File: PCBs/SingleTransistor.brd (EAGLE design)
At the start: 17.8 x 29.2 mm, 4 parts, among them T1 BC547N

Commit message: Updated
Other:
- board size 17.8 x 29.2 mm -> 20.5 x 32.5 mm
- board text added: "PinwheelRobotics"
- board text added: "care@pinwheel.in"
- board text removed: "Pinwheel Robotics"
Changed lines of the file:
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@@
 <drawing>
 <settings>
-<setting alwaysvectorfont="no"/>
+<setting alwaysvectorfont="yes"/>
 <setting verticaltext="up"/>
 </settings>
-<grid distance="50" unitdist="mil" unit="mm" style="lines" multiple="1" display="yes" altdistance="5" altunitdist="mil" altunit="mm"/>
+<grid distance="0.5" unitdist="mm" unit="mm" style="lines" multiple="1" display="yes" altdistance="5" altunitdist="mil" altunit="mm"/>
 <layers>
 <layer number="1" name="Top" color="4" fill="1" visible="yes" active="yes"/>
@@
 <layer number="43" name="vRestrict" color="2" fill="10" visible="yes" active="yes"/>
 <layer number="44" name="Drills" color="7" fill="1" visible="no" active="yes"/>
-<layer number="45" name="Holes" color="7" fill="1" visible="no" active="yes"/>
+<layer number="45" name="Holes" color="7" fill="1" visible="yes" active="yes"/>
 <layer number="46" name="Milling" color="3" fill="1" visible="no" active="yes"/>
 <layer number="47" name="Measures" color="7" fill="1" visible="no" active="yes"/>
@@
 <board>
 <plain>
-<wire x1="2.54" y1="12.7" x2="20.371" y2="12.7" width="0" layer="20"/>
-<wire x1="20.371" y1="12.7" x2="20.371" y2="41.9" width="0" layer="20"/>
-<wire x1="20.371" y1="41.9" x2="2.54" y2="41.9" width="0" layer="20"/>
-<wire x1="2.54" y1="41.9" x2="2.54" y2="12.7" width="0" layer="20"/>
+<wire x1="2.54" y1="42.3052125" x2="2.54" y2="11.949340625" width="0" layer="20"/>
+<wire x1="2.54" y1="11.949340625" x2="3.489340625" y2="11" width="0" layer="20" curve="90"/>
+<wire x1="3.489340625" y1="11" x2="22.0277625" y2="11" width="0" layer="20"/>
+<wire x1="22.0277625" y1="11" x2="23" y2="11.9722375" width="0" layer="20" curve="90"/>
+<wire x1="23" y1="11.9722375" x2="23" y2="42.0655125" width="0" layer="20"/>
+<wire x1="23" y1="42.0655125" x2="21.5655125" y2="43.5" width="0" layer="20" curve="90"/>
+<wire x1="21.5655125" y1="43.5" x2="3.7347875" y2="43.5" width="0" layer="20"/>
+<wire x1="3.7347875" y1="43.5" x2="2.54" y2="42.3052125" width="0" layer="20" curve="90"/>
 <text x="12.7" y="20.574" size="1.778" layer="21">E</text>
 <text x="12.827" y="29.337" size="1.778" layer="21">B</text>
 <text x="12.446" y="38.227" size="1.778" layer="21">C</text>
-<text x="17.399" y="18.161" size="0.6096" layer="21" rot="R90">Pinwheel
-Robotics</text>
+<hole x="4.445" y="41.529" drill="3"/>
+<hole x="20.783" y="41.423" drill="3"/>
+<hole x="20.981" y="12.984" drill="3"/>
+<hole x="4.479" y="12.976" drill="3"/>
+<text x="21.971" y="18.542" size="1.778" layer="21" rot="R90">PinwheelRobotics</text>
+<text x="21.971" y="37.465" size="1.778" layer="22" rot="MR270">care@pinwheel.in</text>
 </plain>
 <attributes>
@@
 </board>
 </drawing>
-<compatibility>
-<note version="6.3" minversion="6.2.2" severity="warning">
-Since Version 6.2.2 text objects can contain more than one line,
-which will not be processed correctly with this version.
-</note>
-</compatibility>
 </eagle>

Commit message: New Update
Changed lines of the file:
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@@
 <drawing>
 <settings>
-<setting alwaysvectorfont="yes"/>
+<setting alwaysvectorfont="no"/>
 <setting verticaltext="up"/>
 </settings>
@@
 <text x="12.827" y="29.337" size="1.778" layer="21">B</text>
 <text x="12.446" y="38.227" size="1.778" layer="21">C</text>
-<hole x="4.445" y="41.529" drill="3"/>
-<hole x="20.783" y="41.423" drill="3"/>
-<hole x="20.981" y="12.984" drill="3"/>
-<hole x="4.479" y="12.976" drill="3"/>
+<hole x="4.5" y="41.5" drill="3"/>
+<hole x="21" y="41.5" drill="3"/>
+<hole x="21" y="13" drill="3"/>
+<hole x="4.5" y="13" drill="3"/>
 <text x="21.971" y="18.542" size="1.778" layer="21" rot="R90">PinwheelRobotics</text>
 <text x="21.971" y="37.465" size="1.778" layer="22" rot="MR270">care@pinwheel.in</text>

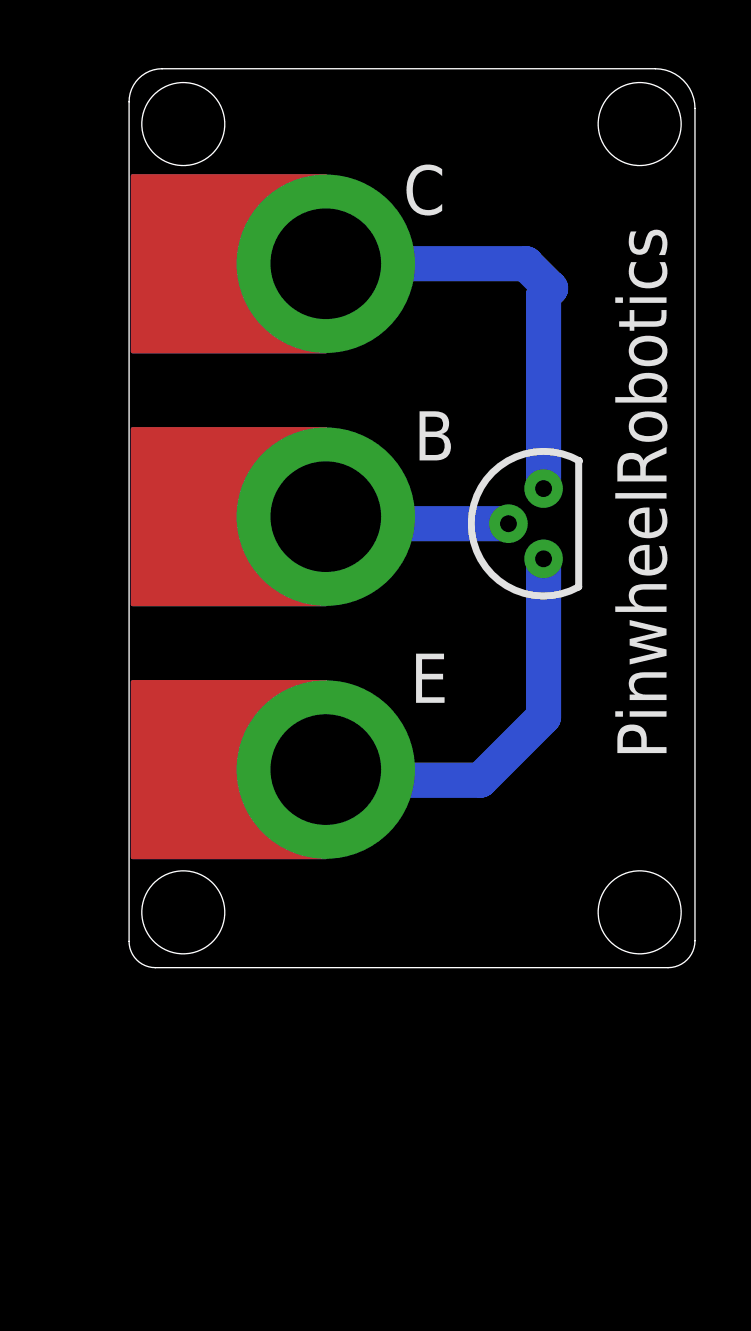
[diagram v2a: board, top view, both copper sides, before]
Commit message: Dimension added
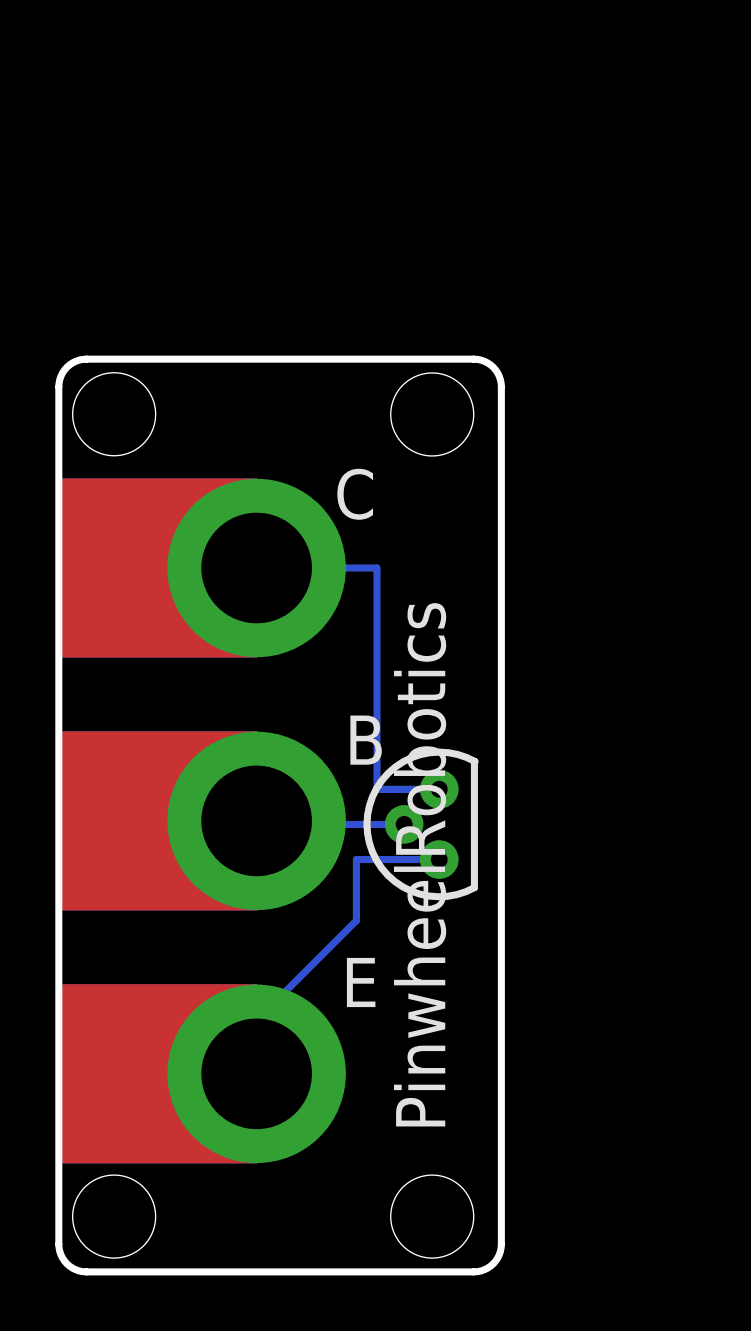
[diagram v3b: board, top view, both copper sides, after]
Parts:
- moved T1 11.5 mm to (13.8, 14.9)
- moved U$3 11.3 mm to (7.15, 7.16)
- moved U$2 11.3 mm to (7.15, 16.3)
- moved U$1 11.3 mm to (7.15, 25.4)
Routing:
- net N$1: track 14.5 -> 12.7 mm
- net N$3: track 16.1 -> 14.6 mm
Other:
- board size 20.5 x 32.5 mm -> 16 x 33 mm
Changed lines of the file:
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@@
 <drawing>
 <settings>
-<setting alwaysvectorfont="no"/>
+<setting alwaysvectorfont="yes"/>
 <setting verticaltext="up"/>
 </settings>
@@
 <board>
 <plain>
-<wire x1="2.54" y1="42.3052125" x2="2.54" y2="11.949340625" width="0" layer="20"/>
-<wire x1="2.54" y1="11.949340625" x2="3.489340625" y2="11" width="0" layer="20" curve="90"/>
-<wire x1="3.489340625" y1="11" x2="22.0277625" y2="11" width="0" layer="20"/>
-<wire x1="22.0277625" y1="11" x2="23" y2="11.9722375" width="0" layer="20" curve="90"/>
-<wire x1="23" y1="11.9722375" x2="23" y2="42.0655125" width="0" layer="20"/>
-<wire x1="23" y1="42.0655125" x2="21.5655125" y2="43.5" width="0" layer="20" curve="90"/>
-<wire x1="21.5655125" y1="43.5" x2="3.7347875" y2="43.5" width="0" layer="20"/>
-<wire x1="3.7347875" y1="43.5" x2="2.54" y2="42.3052125" width="0" layer="20" curve="90"/>
-<text x="12.7" y="20.574" size="1.778" layer="21">E</text>
-<text x="12.827" y="29.337" size="1.778" layer="21">B</text>
-<text x="12.446" y="38.227" size="1.778" layer="21">C</text>
-<hole x="4.5" y="41.5" drill="3"/>
-<hole x="21" y="41.5" drill="3"/>
-<hole x="21" y="13" drill="3"/>
-<hole x="4.5" y="13" drill="3"/>
-<text x="21.971" y="18.542" size="1.778" layer="21" rot="R90">PinwheelRobotics</text>
-<text x="21.971" y="37.465" size="1.778" layer="22" rot="MR270">care@pinwheel.in</text>
+<text x="10.2" y="9.574" size="1.778" layer="21">E</text>
+<text x="10.327" y="18.337" size="1.778" layer="21">B</text>
+<text x="9.946" y="27.227" size="1.778" layer="21">C</text>
+<hole x="2" y="31.008" drill="3"/>
+<hole x="13.5" y="31" drill="3"/>
+<hole x="13.5" y="2" drill="3"/>
+<hole x="2" y="2" drill="3"/>
+<text x="13.971" y="5.042" size="1.778" layer="21" rot="R90">PinwheelRobotics</text>
+<text x="4.471" y="25.465" size="1.778" layer="22" rot="MR270">care@pinwheel.in</text>
+<wire x1="0" y1="1" x2="0" y2="32" width="0.254" layer="20"/>
+<wire x1="0" y1="32" x2="1" y2="33" width="0.254" layer="20" curve="-90"/>
+<wire x1="1" y1="33" x2="15" y2="33" width="0.254" layer="20"/>
+<wire x1="15" y1="33" x2="16" y2="32" width="0.254" layer="20" curve="-90"/>
+<wire x1="16" y1="32" x2="16" y2="1" width="0.254" layer="20"/>
+<wire x1="16" y1="1" x2="15" y2="0" width="0.254" layer="20" curve="-90"/>
+<wire x1="15" y1="0" x2="1" y2="0" width="0.254" layer="20"/>
+<wire x1="1" y1="0" x2="0" y2="1" width="0.254" layer="20" curve="-90"/>
 </plain>
 <attributes>
@@
 </autorouter>
 <elements>
-<element name="T1" library="BC547" package="TO92" value="BC547N" x="17.526" y="25.781" smashed="yes" rot="R90">
-<attribute name="AVAILABILITY" value="In Stock" x="20.066" y="48.641" size="1.778" layer="27" rot="R90" display="off"/>
-<attribute name="CHECK_PRICES" value="https://www.snapeda.com/parts/BC547/Onsemi/view-part/?ref=eda" x="20.066" y="48.641" size="1.778" layer="27" rot="R90" display="off"/>
-<attribute name="DESCRIPTION" value=" Trans GP BJT NPN 45V 0.1A 500mW 3-Pin TO-92 T/R " x="20.066" y="48.641" size="1.778" layer="27" rot="R90" display="off"/>
-<attribute name="MF" value="ON Semiconductor" x="20.066" y="48.641" size="1.778" layer="27" rot="R90" display="off"/>
-<attribute name="MP" value="BC547" x="20.066" y="48.641" size="1.778" layer="27" rot="R90" display="off"/>
-<attribute name="PACKAGE" value="None" x="20.066" y="48.641" size="1.778" layer="27" rot="R90" display="off"/>
-<attribute name="PRICE" value="None" x="20.066" y="48.641" size="1.778" layer="27" rot="R90" display="off"/>
-<attribute name="PURCHASE-URL" value="https://www.snapeda.com/api/url_track_click_mouser/?unipart_id=11254981&amp;manufacturer=ON Semiconductor&amp;part_name=BC547&amp;search_term=None" x="20.066" y="48.641" size="1.778" layer="27" rot="R90" display="off"/>
-<attribute name="SNAPEDA_LINK" value="https://www.snapeda.com/parts/BC547/Onsemi/view-part/?ref=snap" x="20.066" y="48.641" size="1.778" layer="27" rot="R90" display="off"/>
-<attribute name="VALUE" x="15.494" y="40.259" size="1.778" layer="27" rot="R270"/>
+<element name="T1" library="BC547" package="TO92" value="BC547N" x="13.756" y="14.908" smashed="yes" rot="R90">
+<attribute name="AVAILABILITY" value="In Stock" x="16.296" y="37.768" size="1.778" layer="27" rot="R90" display="off"/>
+<attribute name="CHECK_PRICES" value="https://www.snapeda.com/parts/BC547/Onsemi/view-part/?ref=eda" x="16.296" y="37.768" size="1.778" layer="27" rot="R90" display="off"/>
+<attribute name="DESCRIPTION" value=" Trans GP BJT NPN 45V 0.1A 500mW 3-Pin TO-92 T/R " x="16.296" y="37.768" size="1.778" layer="27" rot="R90" display="off"/>
+<attribute name="MF" value="ON Semiconductor" x="16.296" y="37.768" size="1.778" layer="27" rot="R90" display="off"/>
+<attribute name="MP" value="BC547" x="16.296" y="37.768" size="1.778" layer="27" rot="R90" display="off"/>
+<attribute name="PACKAGE" value="None" x="16.296" y="37.768" size="1.778" layer="27" rot="R90" display="off"/>
+<attribute name="PRICE" value="None" x="16.296" y="37.768" size="1.778" layer="27" rot="R90" display="off"/>
+<attribute name="PURCHASE-URL" value="https://www.snapeda.com/api/url_track_click_mouser/?unipart_id=11254981&amp;manufacturer=ON Semiconductor&amp;part_name=BC547&amp;search_term=None" x="16.296" y="37.768" size="1.778" layer="27" rot="R90" display="off"/>
+<attribute name="SNAPEDA_LINK" value="https://www.snapeda.com/parts/BC547/Onsemi/view-part/?ref=snap" x="16.296" y="37.768" size="1.778" layer="27" rot="R90" display="off"/>
+<attribute name="VALUE" x="10.962" y="18.337" size="0.8128" layer="27" rot="R270"/>
 </element>
-<element name="U$1" library="microbit" package="MICROBIT_PAD" value="MICROBIT_PAD" x="9.652" y="36.449" smashed="yes" rot="R270"/>
-<element name="U$2" library="microbit" package="MICROBIT_PAD" value="MICROBIT_PAD" x="9.652" y="27.305" smashed="yes" rot="R270"/>
-<element name="U$3" library="microbit" package="MICROBIT_PAD" value="MICROBIT_PAD" x="9.652" y="18.161" smashed="yes" rot="R270"/>
+<element name="U$1" library="microbit" package="MICROBIT_PAD" value="MICROBIT_PAD" x="7.152" y="25.449" smashed="yes" rot="R270"/>
+<element name="U$2" library="microbit" package="MICROBIT_PAD" value="MICROBIT_PAD" x="7.152" y="16.305" smashed="yes" rot="R270"/>
+<element name="U$3" library="microbit" package="MICROBIT_PAD" value="MICROBIT_PAD" x="7.152" y="7.161" smashed="yes" rot="R270"/>
 </elements>
 <signals>
@@
 <contactref element="U$3" pad="PAD"/>
 <contactref element="T1" pad="1"/>
-<wire x1="17.2212" y1="25.7556" x2="17.526" y2="25.7556" width="0.1524" layer="16"/>
-<wire x1="17.526" y1="25.7556" x2="17.526" y2="25.781" width="0.1524" layer="16"/>
-<wire x1="9.7536" y1="18.288" x2="9.652" y2="18.161" width="0.1524" layer="16"/>
-<wire x1="17.526" y1="25.781" x2="17.526" y2="20.066" width="1.27" layer="16"/>
-<wire x1="17.526" y1="20.066" x2="15.24" y2="17.78" width="1.27" layer="16"/>
-<wire x1="15.24" y1="17.78" x2="10.16" y2="17.78" width="1.27" layer="16"/>
-<wire x1="9.652" y1="18.161" x2="10.16" y2="17.78" width="0" layer="19" extent="16-16"/>
+<wire x1="13.756" y1="14.908" x2="10.7588" y2="14.908" width="0.254" layer="16"/>
+<wire x1="7.152" y1="9.8661" x2="7.152" y2="7.161" width="0.254" layer="16"/>
+<wire x1="10.7588" y1="14.908" x2="10.7588" y2="12.6982" width="0.254" layer="16"/>
+<wire x1="10.7588" y1="12.6982" x2="7.9267" y2="9.8661" width="0.254" layer="16"/>
+<wire x1="7.9267" y1="9.8661" x2="7.152" y2="9.8661" width="0.254" layer="16"/>
 </signal>
 <signal name="N$2">
 <contactref element="T1" pad="2"/>
 <contactref element="U$2" pad="PAD"/>
-<wire x1="9.7536" y1="27.2796" x2="9.906" y2="27.1272" width="0.1524" layer="16"/>
-<wire x1="16.1544" y1="27.1272" x2="16.256" y2="27.051" width="0.1524" layer="16"/>
-<wire x1="9.7536" y1="27.2796" x2="9.652" y2="27.305" width="0.1524" layer="16"/>
-<wire x1="16.256" y1="27.051" x2="11.811" y2="27.051" width="1.27" layer="16"/>
-<wire x1="11.811" y1="27.051" x2="11.43" y2="26.67" width="1.27" layer="16"/>
-<wire x1="9.906" y1="27.1272" x2="11.43" y2="26.67" width="0" layer="19" extent="16-16"/>
+<wire x1="12.486" y1="16.178" x2="7.152" y2="16.178" width="0.254" layer="16"/>
+<wire x1="7.152" y1="16.178" x2="7.152" y2="16.305" width="0.254" layer="16"/>
 </signal>
 <signal name="N$3">
 <contactref element="T1" pad="3"/>
 <contactref element="U$1" pad="PAD"/>
-<wire x1="17.526" y1="28.3464" x2="17.526" y2="28.321" width="0.1524" layer="16"/>
-<wire x1="9.4488" y1="36.4236" x2="9.652" y2="36.449" width="0.1524" layer="16"/>
-<wire x1="17.526" y1="28.321" x2="17.526" y2="35.306" width="1.27" layer="16"/>
-<wire x1="17.526" y1="35.306" x2="17.78" y2="35.56" width="1.27" layer="16"/>
-<wire x1="17.78" y1="35.56" x2="16.891" y2="36.449" width="1.27" layer="16"/>
-<wire x1="16.891" y1="36.449" x2="9.652" y2="36.449" width="1.27" layer="16"/>
+<wire x1="7.152" y1="25.449" x2="11.5" y2="25.449" width="0.254" layer="16"/>
+<wire x1="11.5" y1="17.448" x2="13.756" y2="17.448" width="0.254" layer="16"/>
+<wire x1="11.5" y1="25.449" x2="11.5" y2="17.448" width="0.254" layer="16"/>
 </signal>
 </signals>
